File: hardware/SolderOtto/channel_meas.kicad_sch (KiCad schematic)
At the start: 63 parts, among them Q901 BC847A, Q902 BC858B, Q903 BC847A, U901 OP07, U902 LM358, U903 74hc4053, U904 OP07, U905 OP07

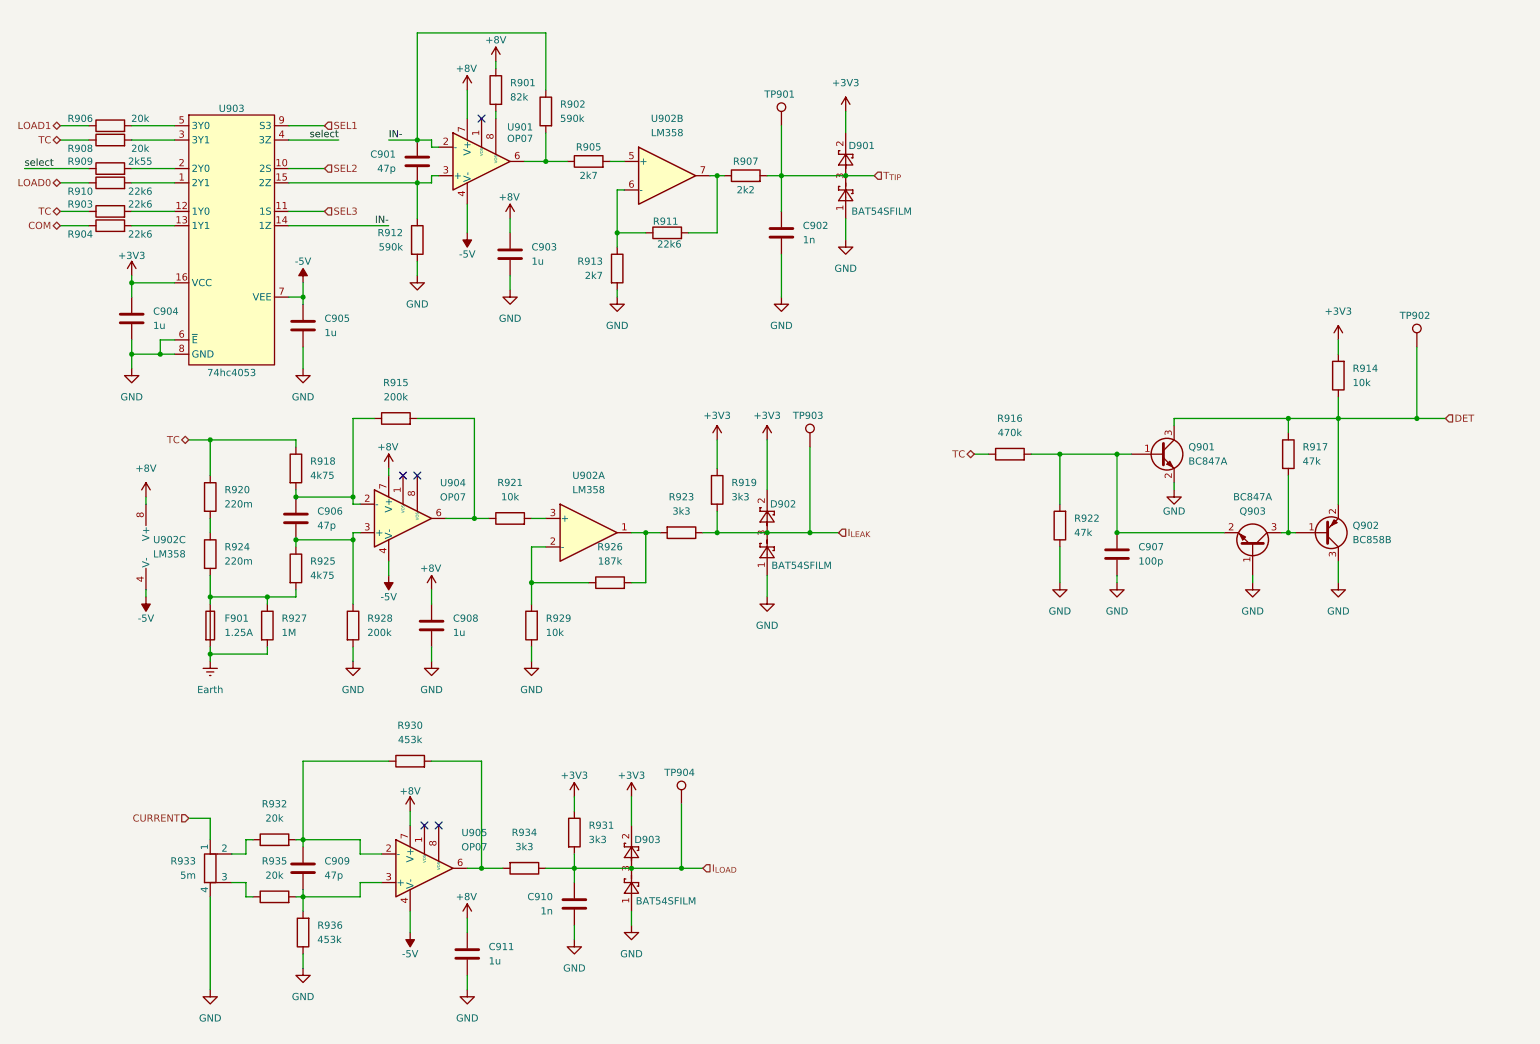
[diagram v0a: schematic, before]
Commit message: try to replace op07c
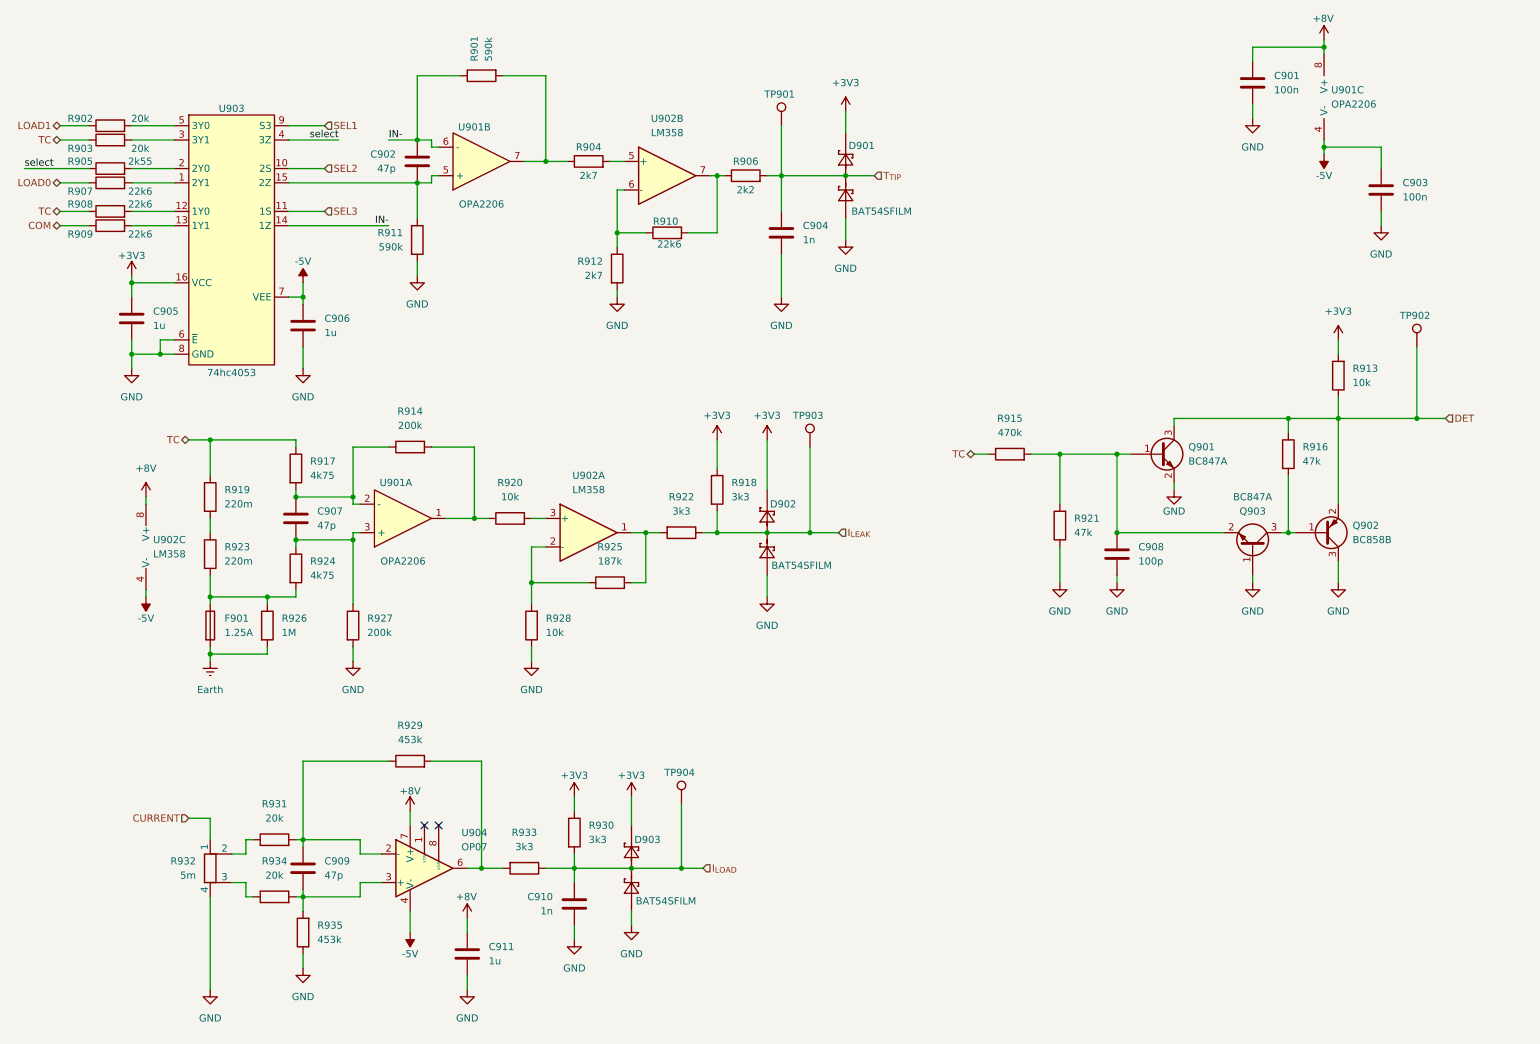
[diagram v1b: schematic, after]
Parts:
- removed C908: 1u, Capacitor_SMD:C_0603_1608Metric, symbol Device:C
- removed R901: 82k, Resistor_SMD:R_0603_1608Metric, symbol Device:R
- removed U901, U904: OP07, Package_SO:SOIC-8_3.9x4.9mm_P1.27mm, symbol mylib_ic:OP07
- added C901: 100n, Capacitor_SMD:C_0603_1608Metric, symbol Device:C
- added U901: OPA2206, Package_SO:VSSOP-8_3x3mm_P0.65mm, symbol mylib_ic:OPA2206
- C903: value 1u -> 100n; Digikey 1276-1184-1-ND -> 1276-1000-1-ND
- renumbered C901 to C902, C902 to C904, C904 to C905, C905 to C906, C906 to C907, C907 to C908, R902 to R901, R906 to R902, R908 to R903, R905 to R904, R909 to R905, R907 to R906, R910 to R907, R903 to R908, R904 to R909, R911 to R910, R912 to R911, R913 to R912, R914 to R913, R915 to R914, R916 to R915, R917 to R916, R918 to R917, R919 to R918, R920 to R919, R921 to R920, R922 to R921, R923 to R922, R924 to R923, R925 to R924, R926 to R925, R927 to R926, R928 to R927, R929 to R928, R930 to R929, R931 to R930, R932 to R931, R933 to R932, R934 to R933, R935 to R934, R936 to R935, U905 to U904
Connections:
- net +8V: now also C901.1, U901.8 (V+); no longer C903.1
- net -5V: now also C903.1, U901.4 (V-)
- net GND: now also C901.2
- net IN-: now also U901.6 (-)
- net at C907.1, R914.1, R917.2: now also U901.2 (-)
- net at R914.2, R920.1: now also U901.1
- net at C902.2, R911.1, U903.15 (2Z): now also U901.5 (+)
- net at C907.2, R924.1, R927.1: now also U901.3 (+)
- net at R901.2, R904.1: now also U901.7
- no-connect marks 5 -> 2
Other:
- moved on the sheet: R901, R914

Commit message: save work
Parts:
- removed C911: 1u, Capacitor_SMD:C_0603_1608Metric, symbol Device:C
- removed U904: OP07, Package_SO:SOIC-8_3.9x4.9mm_P1.27mm, symbol mylib_ic:OP07
- added C912, C913: 100n, Capacitor_SMD:C_0603_1608Metric, symbol Device:C
- added U905: OPA206, Package_SO:VSSOP-8_3x3mm_P0.65mm, symbol mylib_ic:OPA206
- U902: value LM358 -> LM358B; footprint Package_SO:SOIC-8_3.9x4.9mm_P1.27mm -> Package_SO:VSSOP-8_3x3mm_P0.65mm; Digikey 296-LM358DRCT-ND -> 296-LM358BIDGKRCT-ND
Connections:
- net +8V: now also C913.1, U905.7 (V+)
- net -5V: now also C912.1, U905.4 (V-)
- net GND: now also C912.2, C913.2
- net at C909.1, R929.1, R931.2: now also U905.2 (-)
- net at C909.2, R934.2, R935.2: now also U905.3 (+)
- net at R929.2, R933.2: now also U905.6
- new net: U905.1 (NC), U905.5 (NC), U905.8 (NC)
- no-connect marks 2 -> 0

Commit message: save work
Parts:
- removed R919: 220m, Resistor_SMD:R_0603_1608Metric, symbol Device:R
- removed U901: OPA2206, Package_SO:VSSOP-8_3x3mm_P0.65mm, symbol mylib_ic:OPA2206
- added C904, C907: 100n, Capacitor_SMD:C_0603_1608Metric, symbol Device:C
- added C910: 1n, Capacitor_SMD:C_0603_1608Metric, symbol Device:C
- added U901, U904: OPA202, Package_SO:VSSOP-8_3x3mm_P0.65mm, symbol mylib_ic:OPA206
- added unit 2 of U905
- R923: value 220m -> 400m; footprint Resistor_SMD:R_0603_1608Metric -> Resistor_SMD:R_1206_3216Metric; Digikey P.22AJCT-ND -> 283-MFHA1206R4000FCCT-ND
- U905: value OPA206 -> OPA202; Field5 (none) -> 296-OPA202IDGKRCT-ND
- renumbered C904 to C903, C907 to C909, C912 to C911, C913 to C912, C909 to C913, C910 to C914, C903 to C915, R915 to R914, R916 to R915, R914 to R916, R921 to R918, R918 to R919, R920 to R921
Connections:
- net +8V: now also C907.1, U901.7 (V+), U904.7 (V+), U905.7 (V+); no longer U905.7 (V+)
- net -5V: now also C904.1, U901.4 (V-), U904.4 (V-), U905.4 (V-); no longer U905.4 (V-)
- net GND: now also C904.2, C907.2, C910.2
- net IN-: now also U901.2 (-)
- net I_{LEAK}: now also C910.1
- net TC: now also R923.1
- net at C909.1, R916.1, R917.2: now also U904.2 (-)
- net at R916.2, R921.1: now also U904.6
- net at C909.2, R924.1, R927.1: now also U904.3 (+)
- net at C902.2, R911.1, U903.15 (2Z): now also U901.3 (+)
- net at R901.2, R904.1: now also U901.6
- new net: U904.1 (NC), U904.5 (NC), U904.8 (NC)
- new net: U901.1 (NC), U901.5 (NC), U901.8 (NC)
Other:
- moved on the sheet: C901, C908, C911, C912, C915, D902, Q901, Q902, Q903, R913, R914, R915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

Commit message: save work
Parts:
- added R920: 220m, Resistor_SMD:R_0805_2012Metric, symbol Device:R
- R923: value 400m -> 220m; footprint Resistor_SMD:R_1206_3216Metric -> Resistor_SMD:R_0805_2012Metric
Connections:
- net TC: now also R920.1; no longer R923.1
- new net: R920.2, R923.1
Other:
- moved on the sheet: R923
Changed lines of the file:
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@@
 	(wire
 		(pts
-			(xy 49.53 92.71) (xy 49.53 102.87)
+			(xy 49.53 92.71) (xy 49.53 97.79)
 		)
 		(stroke
@@
 	(wire
 		(pts
+			(xy 49.53 105.41) (xy 49.53 109.22)
+		)
+		(stroke
+			(width 0)
+			(type default)
+		)
+	)
+	(wire
+		(pts
 			(xy 63.5 44.45) (xy 69.85 44.45)
 		)
@@
 	(wire
 		(pts
-			(xy 49.53 110.49) (xy 49.53 120.65)
+			(xy 49.53 116.84) (xy 49.53 120.65)
 		)
 		(stroke
@@
 	)
 	(symbol
+		(lib_id "Device:R")
+		(at 49.53 101.6 0)
+		(unit 1)
+		(exclude_from_sim no)
+		(in_bom yes)
+		(on_board yes)
+		(dnp no)
+		(fields_autoplaced yes)
+		(property "Reference" "R920"
+			(at 52.07 100.3299 0)
+			(effects
+				(font
+					(size 1.27 1.27)
+				)
+				(justify left)
+			)
+		)
+		(property "Value" "220m"
+			(at 52.07 102.8699 0)
+			(effects
+				(font
+					(size 1.27 1.27)
+				)
+				(justify left)
+			)
+		)
+		(property "Footprint" "Resistor_SMD:R_0805_2012Metric"
+			(at 47.752 101.6 90)
+			(effects
+				(font
+					(size 1.27 1.27)
+				)
+				(hide yes)
+			)
+		)
+		(property "Datasheet" "~"
+			(at 49.53 101.6 0)
+			(effects
+				(font
+					(size 1.27 1.27)
+				)
+				(hide yes)
+			)
+		)
+		(property "Description" "Resistor"
+			(at 49.53 101.6 0)
+			(effects
+				(font
+					(size 1.27 1.27)
+				)
+				(hide yes)
+			)
+		)
+		(property "Digikey" "P19292CT-ND"
+			(at 49.53 101.6 0)
+			(effects
+				(font
+					(size 1.27 1.27)
+				)
+				(hide yes)
+			)
+		)
+		(pin "2"
+		)
+		(pin "1"
+		)
+		(instances
+			(project "SolderOtto"
+				(path "/04e99464-bf33-4a4f-8397-d26b5ec904f3/57a4c2b0-a7ab-4dc9-9bcc-6bd7e1b882d1/1807ce44-453b-46b0-b8fc-698b650e1609"
+					(reference "R920")
+					(unit 1)
+				)
+			)
+		)
+	)
+	(symbol
 		(lib_id "Connector:TestPoint")
 		(at 151.13 36.83 0)
@@
 	(symbol
 		(lib_id "Device:R")
-		(at 49.53 106.68 0)
+		(at 49.53 113.03 0)
 		(unit 1)
 		(exclude_from_sim no)
@@
 		(fields_autoplaced yes)
 		(property "Reference" "R923"
-			(at 52.07 105.4099 0)
+			(at 52.07 111.7599 0)
 			(effects
 				(font
@@
 			)
 		)
-		(property "Value" "400m"
-			(at 52.07 107.9499 0)
+		(property "Value" "220m"
+			(at 52.07 114.2999 0)
 			(effects
 				(font
@@
 			)
 		)
-		(property "Footprint" "Resistor_SMD:R_1206_3216Metric"
-			(at 47.752 106.68 90)
+		(property "Footprint" "Resistor_SMD:R_0805_2012Metric"
+			(at 47.752 113.03 90)
 			(effects
 				(font
@@
 		)
 		(property "Datasheet" "~"
-			(at 49.53 106.68 0)
+			(at 49.53 113.03 0)
 			(effects
 				(font
@@
 		)
 		(property "Description" "Resistor"
-			(at 49.53 106.68 0)
+			(at 49.53 113.03 0)
 			(effects
 				(font
@@
 		)
 		(property "Digikey" "283-MFHA1206R4000FCCT-ND"
-			(at 49.53 106.68 0)
+			(at 49.53 113.03 0)
 			(effects
 				(font

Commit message: save work
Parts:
- renumbered R920 to R919, R919 to R920
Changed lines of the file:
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@@
 		(dnp no)
 		(fields_autoplaced yes)
-		(property "Reference" "R919"
+		(property "Reference" "R920"
 			(at 142.24 100.3299 0)
 			(effects
@@
 			(project "SolderOtto"
 				(path "/04e99464-bf33-4a4f-8397-d26b5ec904f3/57a4c2b0-a7ab-4dc9-9bcc-6bd7e1b882d1/1807ce44-453b-46b0-b8fc-698b650e1609"
-					(reference "R919")
+					(reference "R920")
 					(unit 1)
 				)
@@
 		(dnp no)
 		(fields_autoplaced yes)
-		(property "Reference" "R920"
+		(property "Reference" "R919"
 			(at 52.07 100.3299 0)
 			(effects
@@
 			(project "SolderOtto"
 				(path "/04e99464-bf33-4a4f-8397-d26b5ec904f3/57a4c2b0-a7ab-4dc9-9bcc-6bd7e1b882d1/1807ce44-453b-46b0-b8fc-698b650e1609"
-					(reference "R920")
-					(unit 1)
-				)
+					(reference "R919")
+					(unit 1)
+				)

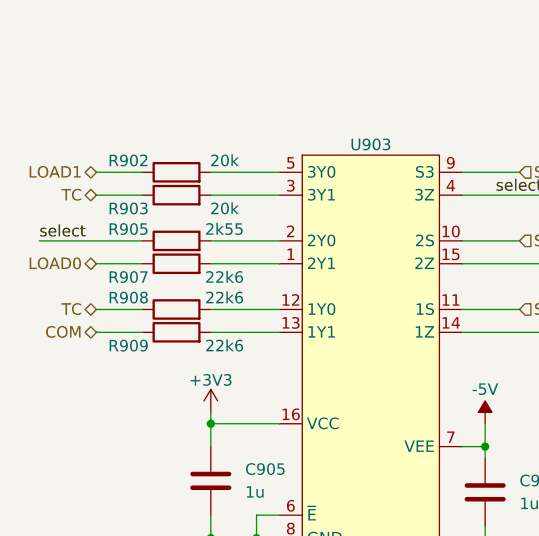
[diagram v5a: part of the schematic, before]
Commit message: add via stichting
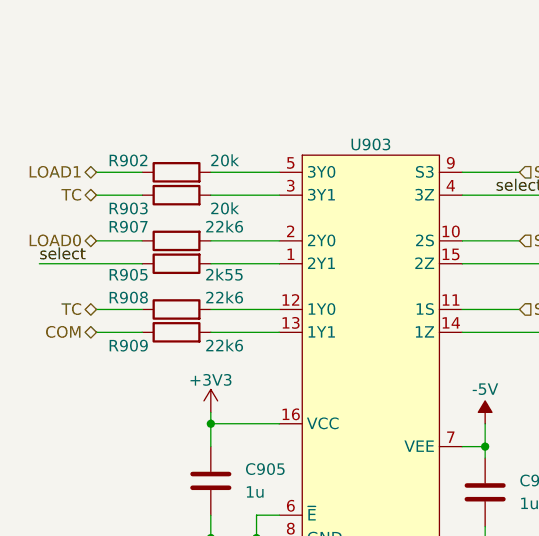
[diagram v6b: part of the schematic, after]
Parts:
- U901, U902, U904, U905: footprint Package_SO:VSSOP-8_3x3mm_P0.65mm -> Package_SO:SOIC-8_3.9x4.9mm_P1.27mm
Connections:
- net at R907.2: now also U903.2 (2Y0); no longer U903.1 (2Y1)
- net at R905.2: now also U903.1 (2Y1); no longer U903.2 (2Y0)
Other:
- moved on the sheet: R905, R907
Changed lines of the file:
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@@
 	(wire
 		(pts
-			(xy 22.86 46.99) (xy 27.94 46.99)
+			(xy 22.86 44.45) (xy 27.94 44.45)
 		)
 		(stroke
@@
 	(wire
 		(pts
-			(xy 16.51 44.45) (xy 27.94 44.45)
+			(xy 16.51 46.99) (xy 27.94 46.99)
 		)
 		(stroke
@@
 	)
 	(label "select"
-		(at 16.51 44.45 0)
+		(at 16.51 46.99 0)
 		(fields_autoplaced yes)
 		(effects
@@
 	(hierarchical_label "LOAD0"
 		(shape bidirectional)
-		(at 22.86 46.99 180)
+		(at 22.86 44.45 180)
 		(fields_autoplaced yes)
 		(effects
@@
 			)
 		)
-		(property "Footprint" "Package_SO:VSSOP-8_3x3mm_P0.65mm"
+		(property "Footprint" "Package_SO:SOIC-8_3.9x4.9mm_P1.27mm"
 			(at 83.82 106.68 0)
 			(effects
@@
 	(symbol
 		(lib_id "Device:R")
-		(at 31.75 46.99 90)
+		(at 31.75 44.45 90)
+		(mirror x)
 		(unit 1)
 		(exclude_from_sim no)
@@
 		(dnp no)
 		(property "Reference" "R907"
-			(at 26.416 48.514 90)
+			(at 26.416 42.926 90)
 			(effects
 				(font
@@
 		)
 		(property "Value" "22k6"
-			(at 37.084 48.514 90)
+			(at 37.084 42.926 90)
 			(effects
 				(font
@@
 		)
 		(property "Footprint" "Resistor_SMD:R_0603_1608Metric"
-			(at 31.75 48.768 90)
+			(at 31.75 42.672 90)
 			(effects
 				(font
@@
 		)
 		(property "Datasheet" "~"
-			(at 31.75 46.99 0)
+			(at 31.75 44.45 0)
 			(effects
 				(font
@@
 		)
 		(property "Description" "Resistor"
-			(at 31.75 46.99 0)
+			(at 31.75 44.45 0)
 			(effects
 				(font
@@
 		)
 		(property "Digikey" "P22.6KHCT-ND"
-			(at 31.75 46.99 0)
+			(at 31.75 44.45 0)
 			(effects
 				(font
@@
 			)
 		)
-		(property "Footprint" "Package_SO:VSSOP-8_3x3mm_P0.65mm"
+		(property "Footprint" "Package_SO:SOIC-8_3.9x4.9mm_P1.27mm"
 			(at 97.79 43.18 0)
 			(effects
@@
 			)
 		)
-		(property "Footprint" "Package_SO:VSSOP-8_3x3mm_P0.65mm"
+		(property "Footprint" "Package_SO:SOIC-8_3.9x4.9mm_P1.27mm"
 			(at 40.64 111.76 0)
 			(effects
@@
 			)
 		)
-		(property "Footprint" "Package_SO:VSSOP-8_3x3mm_P0.65mm"
+		(property "Footprint" "Package_SO:SOIC-8_3.9x4.9mm_P1.27mm"
 			(at 184.15 107.95 0)
 			(effects
@@
 			)
 		)
-		(property "Footprint" "Package_SO:VSSOP-8_3x3mm_P0.65mm"
+		(property "Footprint" "Package_SO:SOIC-8_3.9x4.9mm_P1.27mm"
 			(at 116.84 109.22 0)
 			(effects
@@
 	(symbol
 		(lib_id "Device:R")
-		(at 31.75 44.45 90)
+		(at 31.75 46.99 90)
+		(mirror x)
 		(unit 1)
 		(exclude_from_sim no)
@@
 		(dnp no)
 		(property "Reference" "R905"
-			(at 26.416 43.18 90)
+			(at 26.416 48.26 90)
 			(effects
 				(font
@@
 		)
 		(property "Value" "2k55"
-			(at 37.084 43.18 90)
+			(at 37.084 48.26 90)
 			(effects
 				(font
@@
 		)
 		(property "Footprint" "Resistor_SMD:R_0603_1608Metric"
-			(at 31.75 46.228 90)
+			(at 31.75 45.212 90)
 			(effects
 				(font
@@
 		)
 		(property "Datasheet" "~"
-			(at 31.75 44.45 0)
+			(at 31.75 46.99 0)
 			(effects
 				(font
@@
 		)
 		(property "Description" "Resistor"
-			(at 31.75 44.45 0)
+			(at 31.75 46.99 0)
 			(effects
 				(font
@@
 		)
 		(property "Digikey" "311-2.55KHRCT-ND"
-			(at 31.75 44.45 0)
+			(at 31.75 46.99 0)
 			(effects
 				(font
@@
 			)
 		)
-		(property "Footprint" "Package_SO:VSSOP-8_3x3mm_P0.65mm"
+		(property "Footprint" "Package_SO:SOIC-8_3.9x4.9mm_P1.27mm"
 			(at 177.8 44.45 0)
 			(effects
@@
 			)
 		)
-		(property "Footprint" "Package_SO:VSSOP-8_3x3mm_P0.65mm"
+		(property "Footprint" "Package_SO:SOIC-8_3.9x4.9mm_P1.27mm"
 			(at 130.81 45.72 0)
 			(effects
@@
 			)
 		)
-		(property "Footprint" "Package_SO:VSSOP-8_3x3mm_P0.65mm"
+		(property "Footprint" "Package_SO:SOIC-8_3.9x4.9mm_P1.27mm"
 			(at 86.36 168.91 0)
 			(effects
@@
 			)
 		)
-		(property "Footprint" "Package_SO:VSSOP-8_3x3mm_P0.65mm"
+		(property "Footprint" "Package_SO:SOIC-8_3.9x4.9mm_P1.27mm"
 			(at 154.94 170.18 0)
 			(effects

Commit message: fix some part numbers
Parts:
- D901, D902, D903: Mouser 511-BAT54SFILM -> (none)
- R923: Digikey 283-MFHA1206R4000FCCT-ND -> P19292CT-ND
- U901, U904: Digikey (none) -> 296-51494-1-ND;296-14626-1-ND;296-OPA206ADRCT-ND
- U905: Digikey (none) -> 296-51494-1-ND;296-14626-1-ND;296-OPA206ADRCT-ND; Field5 296-OPA202IDGKRCT-ND -> (none)
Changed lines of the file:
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@@
 			)
 		)
+		(property "Digikey" "296-51494-1-ND;296-14626-1-ND;296-OPA206ADRCT-ND"
+			(at 82.55 106.68 0)
+			(effects
+				(font
+					(size 1.27 1.27)
+				)
+				(hide yes)
+			)
+		)
 		(pin "6"
 		)
@@
 			)
 		)
-		(property "Mouser" "511-BAT54SFILM"
-			(at 164.084 55.118 90)
-			(effects
-				(font
-					(size 1.27 1.27)
-				)
-				(justify right)
-				(hide yes)
-			)
-		)
 		(property "Digikey" "497-2522-1-ND"
 			(at 162.56 45.72 0)
@@
 			)
 		)
+		(property "Digikey" "296-51494-1-ND;296-14626-1-ND;296-OPA206ADRCT-ND"
+			(at 96.52 43.18 0)
+			(effects
+				(font
+					(size 1.27 1.27)
+				)
+				(hide yes)
+			)
+		)
 		(pin "6"
 		)
@@
 			)
 		)
-		(property "Mouser" "511-BAT54SFILM"
-			(at 128.778 168.91 0)
-			(effects
-				(font
-					(size 1.27 1.27)
-				)
-				(hide yes)
-			)
-		)
 		(pin "3"
 		)
@@
 			)
 		)
-		(property "Mouser" "511-BAT54SFILM"
-			(at 149.86 109.22 0)
-			(effects
-				(font
-					(size 1.27 1.27)
-				)
-				(hide yes)
-			)
-		)
 		(pin "3"
 		)
@@
 			)
 		)
+		(property "Digikey" "296-51494-1-ND;296-14626-1-ND;296-OPA206ADRCT-ND"
+			(at 182.88 107.95 0)
+			(effects
+				(font
+					(size 1.27 1.27)
+				)
+				(hide yes)
+			)
+		)
 		(pin "6"
 		)
@@
 			)
 		)
+		(property "Digikey" "296-51494-1-ND;296-14626-1-ND;296-OPA206ADRCT-ND"
+			(at 179.07 44.45 0)
+			(effects
+				(font
+					(size 1.27 1.27)
+				)
+				(hide yes)
+			)
+		)
 		(pin "6"
 		)
@@
 			)
 		)
-		(property "Digikey" "283-MFHA1206R4000FCCT-ND"
+		(property "Digikey" "P19292CT-ND"
 			(at 49.53 113.03 0)
 			(effects
@@
 			)
 		)
-		(property "Field5" "296-OPA202IDGKRCT-ND"
+		(property "Digikey" "296-51494-1-ND;296-14626-1-ND;296-OPA206ADRCT-ND"
 			(at 86.36 168.91 0)
 			(effects
@@
 			)
 		)
-		(property "Field5" "296-OPA202IDGKRCT-ND"
+		(property "Digikey" "296-51494-1-ND;296-14626-1-ND;296-OPA206ADRCT-ND"
 			(at 154.94 170.18 0)
 			(effects
